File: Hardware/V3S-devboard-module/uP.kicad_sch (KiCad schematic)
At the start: 11 parts, among them U1 V3S, Y1 Crystal_GND23_Small, Y2 Crystal_GND23_Small

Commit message: schematic improvements
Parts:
- added C45, C46: 1u, symbol Device:C_Small
- added J2: Micro_SD_Card_Det1, v3s-devboard-module:J_sd_micro_socket, symbol Connector:Micro_SD_Card_Det1
- added L4: 2.2u, symbol Device:L_Small
- added R15, R17: 10K, symbol Device:R_Small_US
- added R16: 47K, symbol Device:R_Small_US
- added RN1: 6x47K, Resistor_THT:R_Array_SIP7, symbol Device:R_Pack06
- added SW1: SW_MEC_5E, mod:SW_SKRPACE010, symbol Switch:SW_MEC_5E
- added U4: W25Q128JVS, Package_SO:SOIC-8_5.23x5.23mm_P1.27mm, symbol Memory_Flash:W25Q128JVS
- added U5: AP3019AKTR-G1, Package_TO_SOT_SMD:SOT-23-6, symbol v3s-devboard-module:AP3019AKTR-G1
- U1: footprint Package_QFP:LQFP-128_14x14mm_P0.4mm -> v3s-devboard-module:LQFP-128_L14.0-W14.0-P0.40-LS16.0-BL-EP5.0
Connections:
- net GND: now also C45.1, C46.1, J2.6 (VSS), R17.1, SW1.3 (K), U4.4 (GND), U5.2 (GND)
- net PF0_SDC0D1_JTAGDI1: now also J2.8 (DAT1), RN1.5 (R5.1)
- net PF1_SDC0D0_JTAGDI1: now also J2.7 (DAT0), RN1.4 (R4.1)
- net PF2_SDC0CLK_UART0TX: now also J2.5 (CLK)
- net PF3_SDC0CMD_JTAGDO1: now also J2.3 (CMD), RN1.3 (R3.1)
- net PF4_SDC0D3_UART0RX: now also J2.2 (DAT3/CD), RN1.2 (R2.1)
- net PF5_SDC0D2_JTAGCK1: now also J2.1 (DAT2), RN1.1 (R1.1)
- net PF6: now also J2.9 (DET), RN1.6 (R6.1)
- net SPI.CLK: now also U4.6 (CLK)
- net SPI.CS: now also R15.1, U4.1 (~{CS})
- net SPI.MISO: now also U4.2 (DO(IO1))
- net SPI.MOSI: now also U4.5 (DI(IO0))
- net UART2.RTS renamed PB2
- net PB2: now also R17.2, U5.4 (CTRL)
- new net: L4.2, U5.1 (SW)
- new net: C46.2, L4.1, U5.6 (VIN)
- new net: C45.2, R16.2, SW1.2
- new net 3V3: J2.4 (VDD), R15.2, R16.1, RN1.10 (R3.2), RN1.11 (R2.2), RN1.12 (R1.2), RN1.7 (R6.2), RN1.8 (R5.2), RN1.9 (R4.2), U4.3 (IO2), U4.7 (IO3), U4.8 (VCC)
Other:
- moved on the sheet: R8, U1

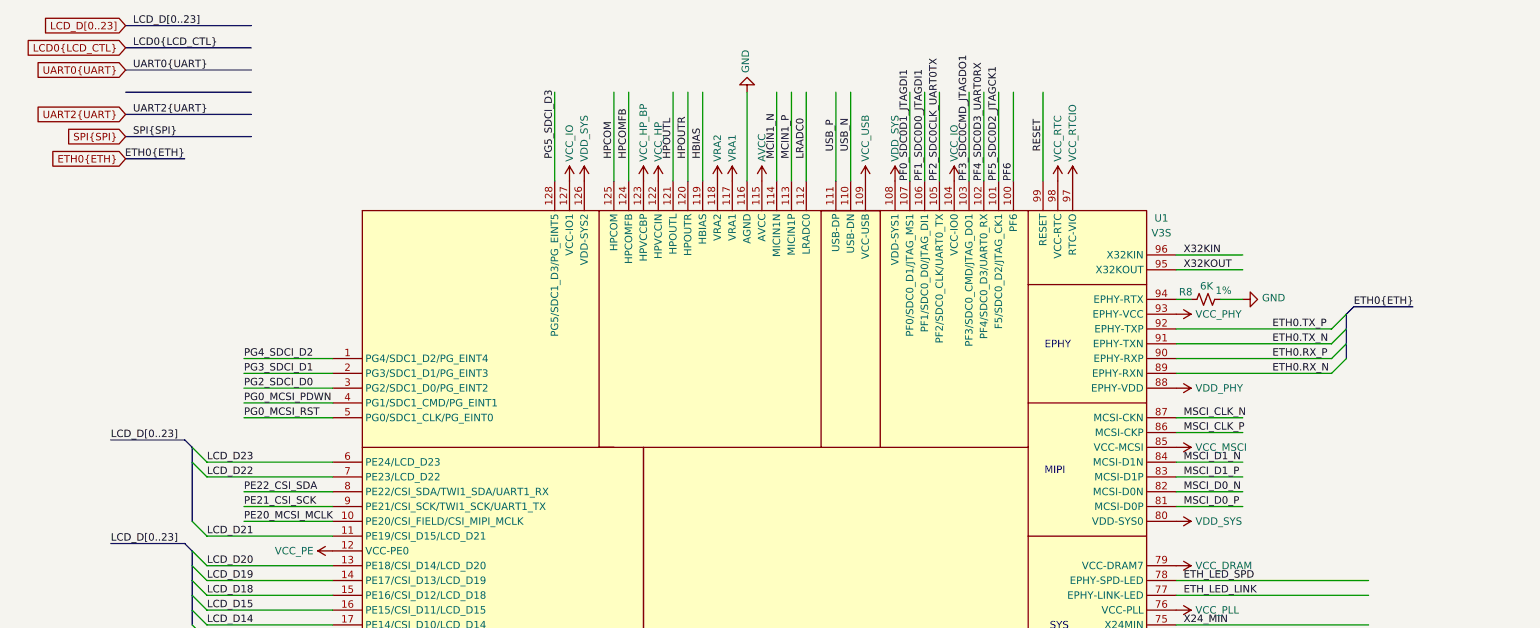
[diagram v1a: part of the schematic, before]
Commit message: Removed old project. Schematic improvements
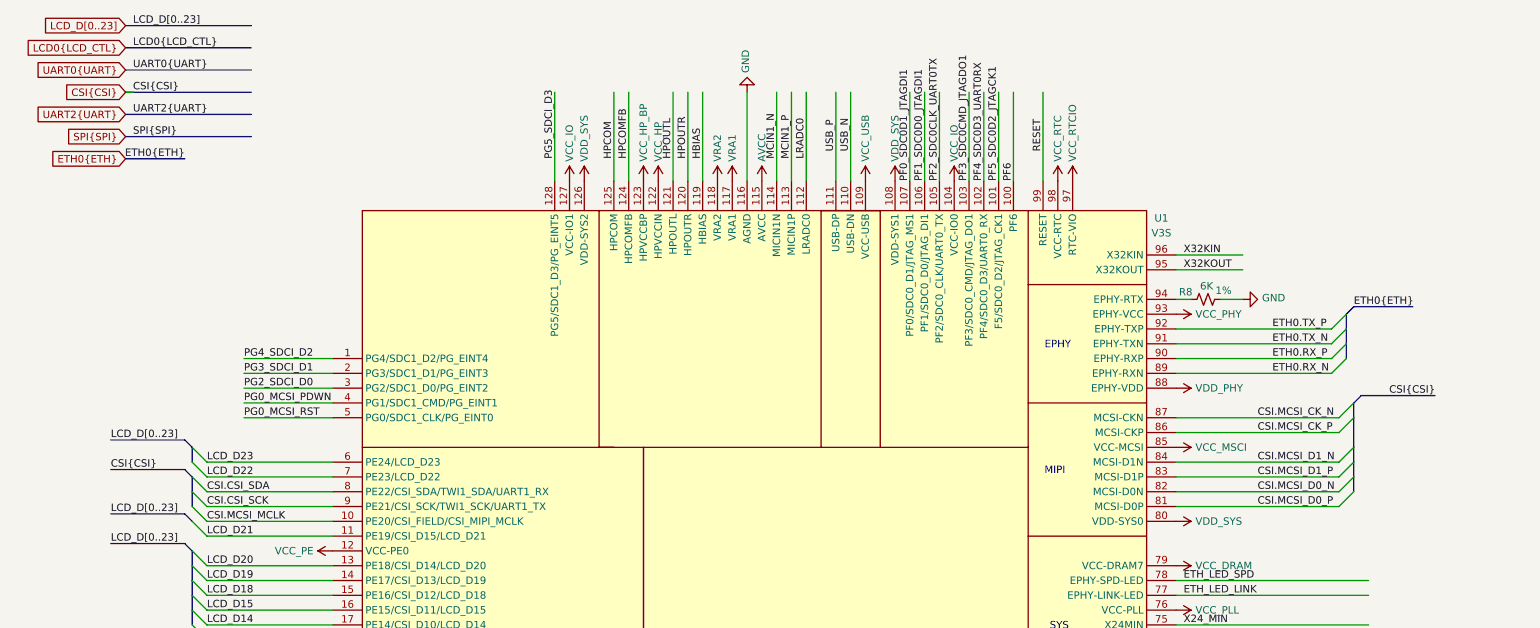
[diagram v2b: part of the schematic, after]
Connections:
- net MSCI_CLK_N renamed CSI.MCSI_CK_N
- net MSCI_CLK_P renamed CSI.MCSI_CK_P
- net MSCI_D0_N renamed CSI.MCSI_D0_N
- net MSCI_D0_P renamed CSI.MCSI_D0_P
- net MSCI_D1_N renamed CSI.MCSI_D1_N
- net MSCI_D1_P renamed CSI.MCSI_D1_P
- net PE20_MCSI_MCLK renamed CSI.MCSI_MCLK
- net PE21_CSI_SCK renamed CSI.CSI_SCK
- net PE22_CSI_SDA renamed CSI.CSI_SDA

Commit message: general improvements. power almost complete
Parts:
- removed C46: 1u, symbol Device:C_Small
- removed L4: 2.2u, symbol Device:L_Small
- removed R17: 10K, symbol Device:R_Small_US
- removed U5: AP3019AKTR-G1, Package_TO_SOT_SMD:SOT-23-6, symbol v3s-devboard-module:AP3019AKTR-G1
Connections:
- net PF0_SDC0D1_JTAGDI1: no longer U1.107 (PF0/SDC0_D1/JTAG_MS1)
- net PF1_SDC0D0_JTAGDI1: no longer U1.106 (PF1/SDC0_D0/JTAG_DI1)
- net PF2_SDC0CLK_UART0TX: no longer U1.105 (PF2/SDC0_CLK/UART0_TX)
- net PF3_SDC0CMD_JTAGDO1: no longer U1.103 (PF3/SDC0_CMD/JTAG_DO1)
- net PF4_SDC0D3_UART0RX: no longer U1.102 (PF4/SDC0_D3/UART0_RX)
- net PF5_SDC0D2_JTAGCK1: no longer U1.101 (F5/SDC0_D2/JTAG_CK1)
- net RESET: now also C45.2, R16.2, SW1.2
- net PG0_MCSI_PDWN renamed SDC1.CMD
- net PG0_MCSI_RST renamed SDC1.CLK
- net PG2_SDCI_D0 renamed SDC1.D0
- net PG3_SDCI_D1 renamed SDC1.D1
- net PG4_SDCI_D2 renamed SDC1.D2
- net USB_N renamed USB.USB_N
- net USB_P renamed USB.USB_P
- new net SDC0.CLK: U1.105 (PF2/SDC0_CLK/UART0_TX)
- new net SDC0.CMD: U1.103 (PF3/SDC0_CMD/JTAG_DO1)
- new net SDC0.D0: U1.106 (PF1/SDC0_D0/JTAG_DI1)
- new net SDC0.D1: U1.107 (PF0/SDC0_D1/JTAG_MS1)
- new net SDC0.D2: U1.101 (F5/SDC0_D2/JTAG_CK1)
- new net SDC0.D3: U1.102 (PF4/SDC0_D3/UART0_RX)
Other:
- note added: "Interfaces: 1xParallel LCD (24bit+ctl) 2xUART 1xSPI 1xCSI (Camera Serial Interface) 2xSDC 1xETH 1xUSB"
- note added: "Use AP3019AKTR-G1 for LCD backlight generation"
- moved on the sheet: R8, U1

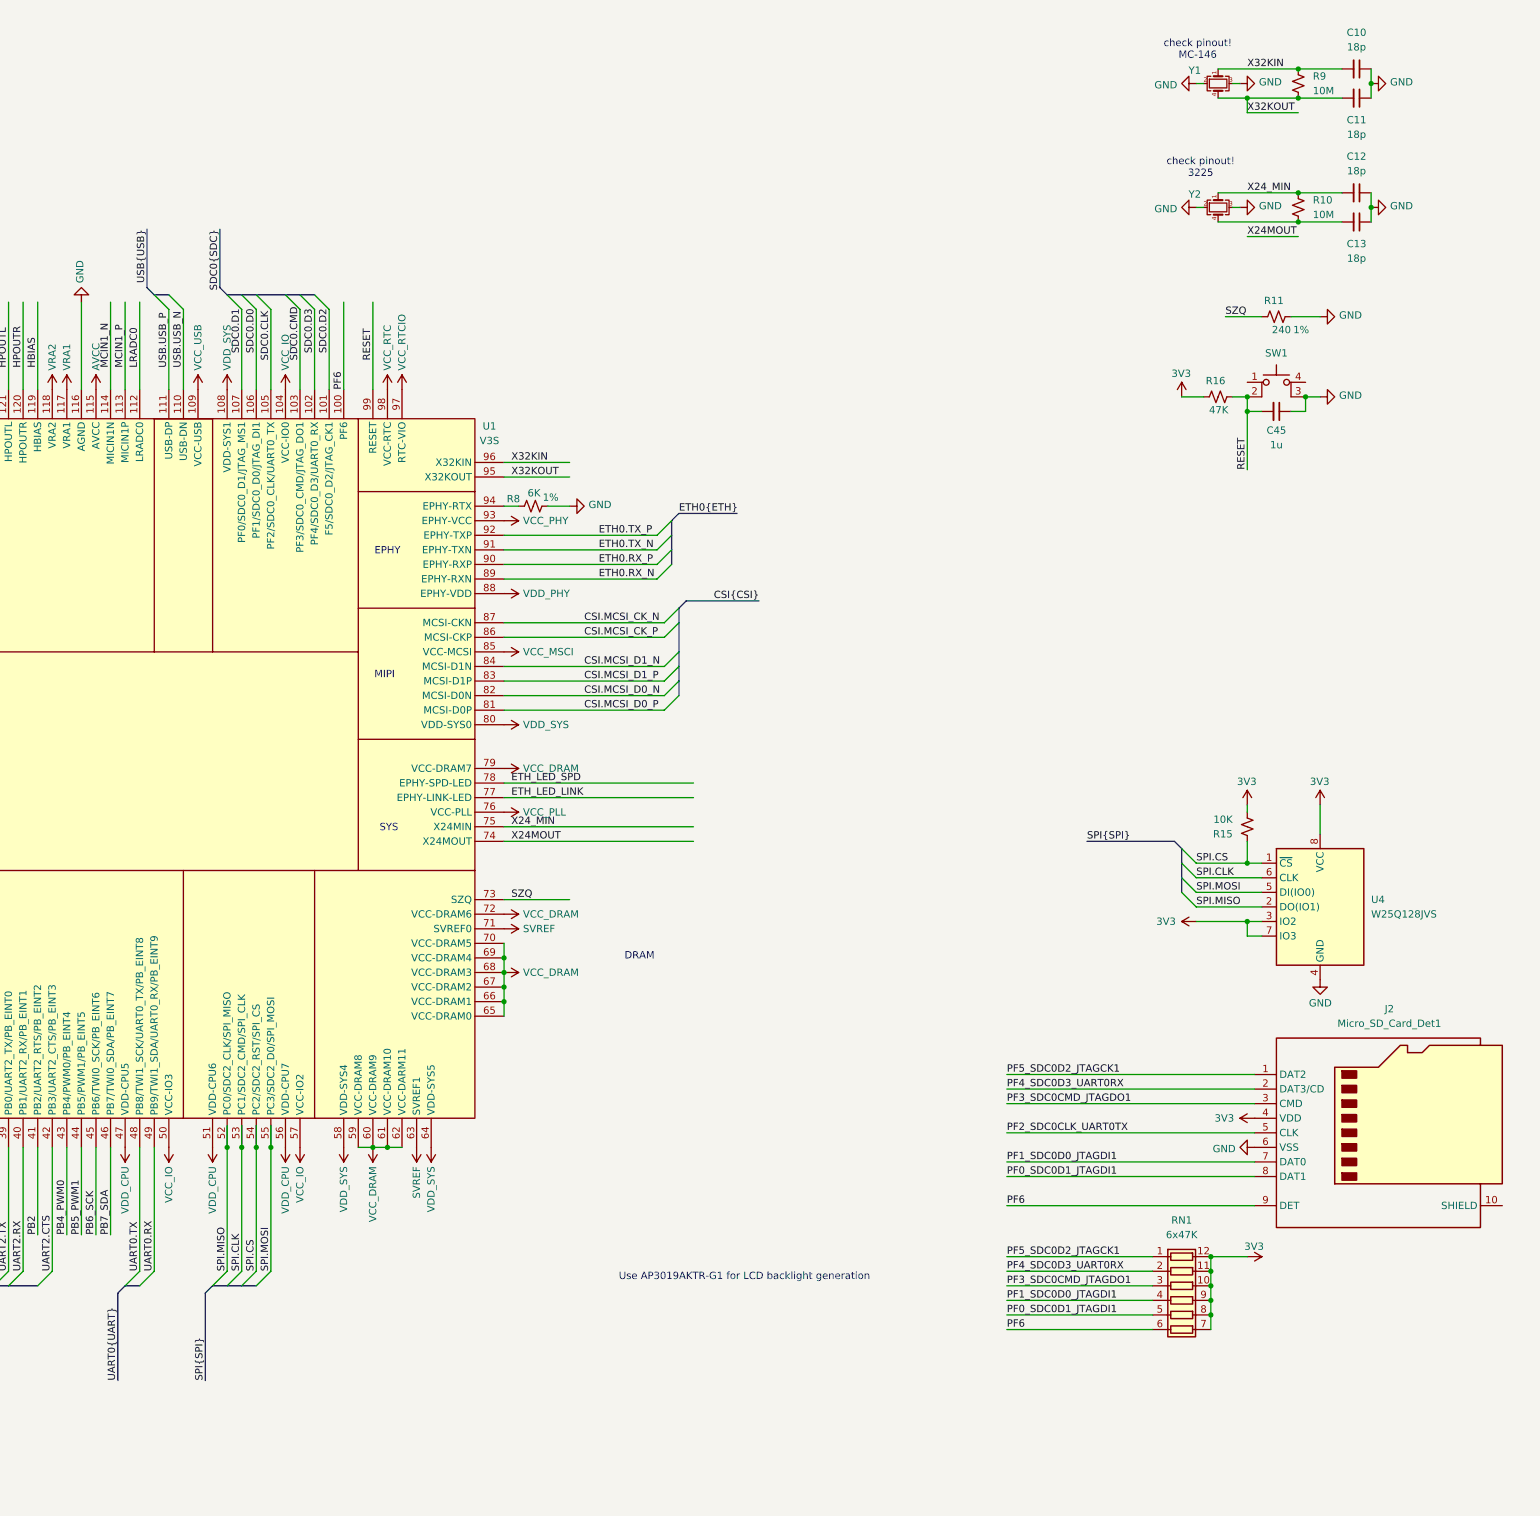
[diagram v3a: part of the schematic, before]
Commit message: CPU schematic improvements
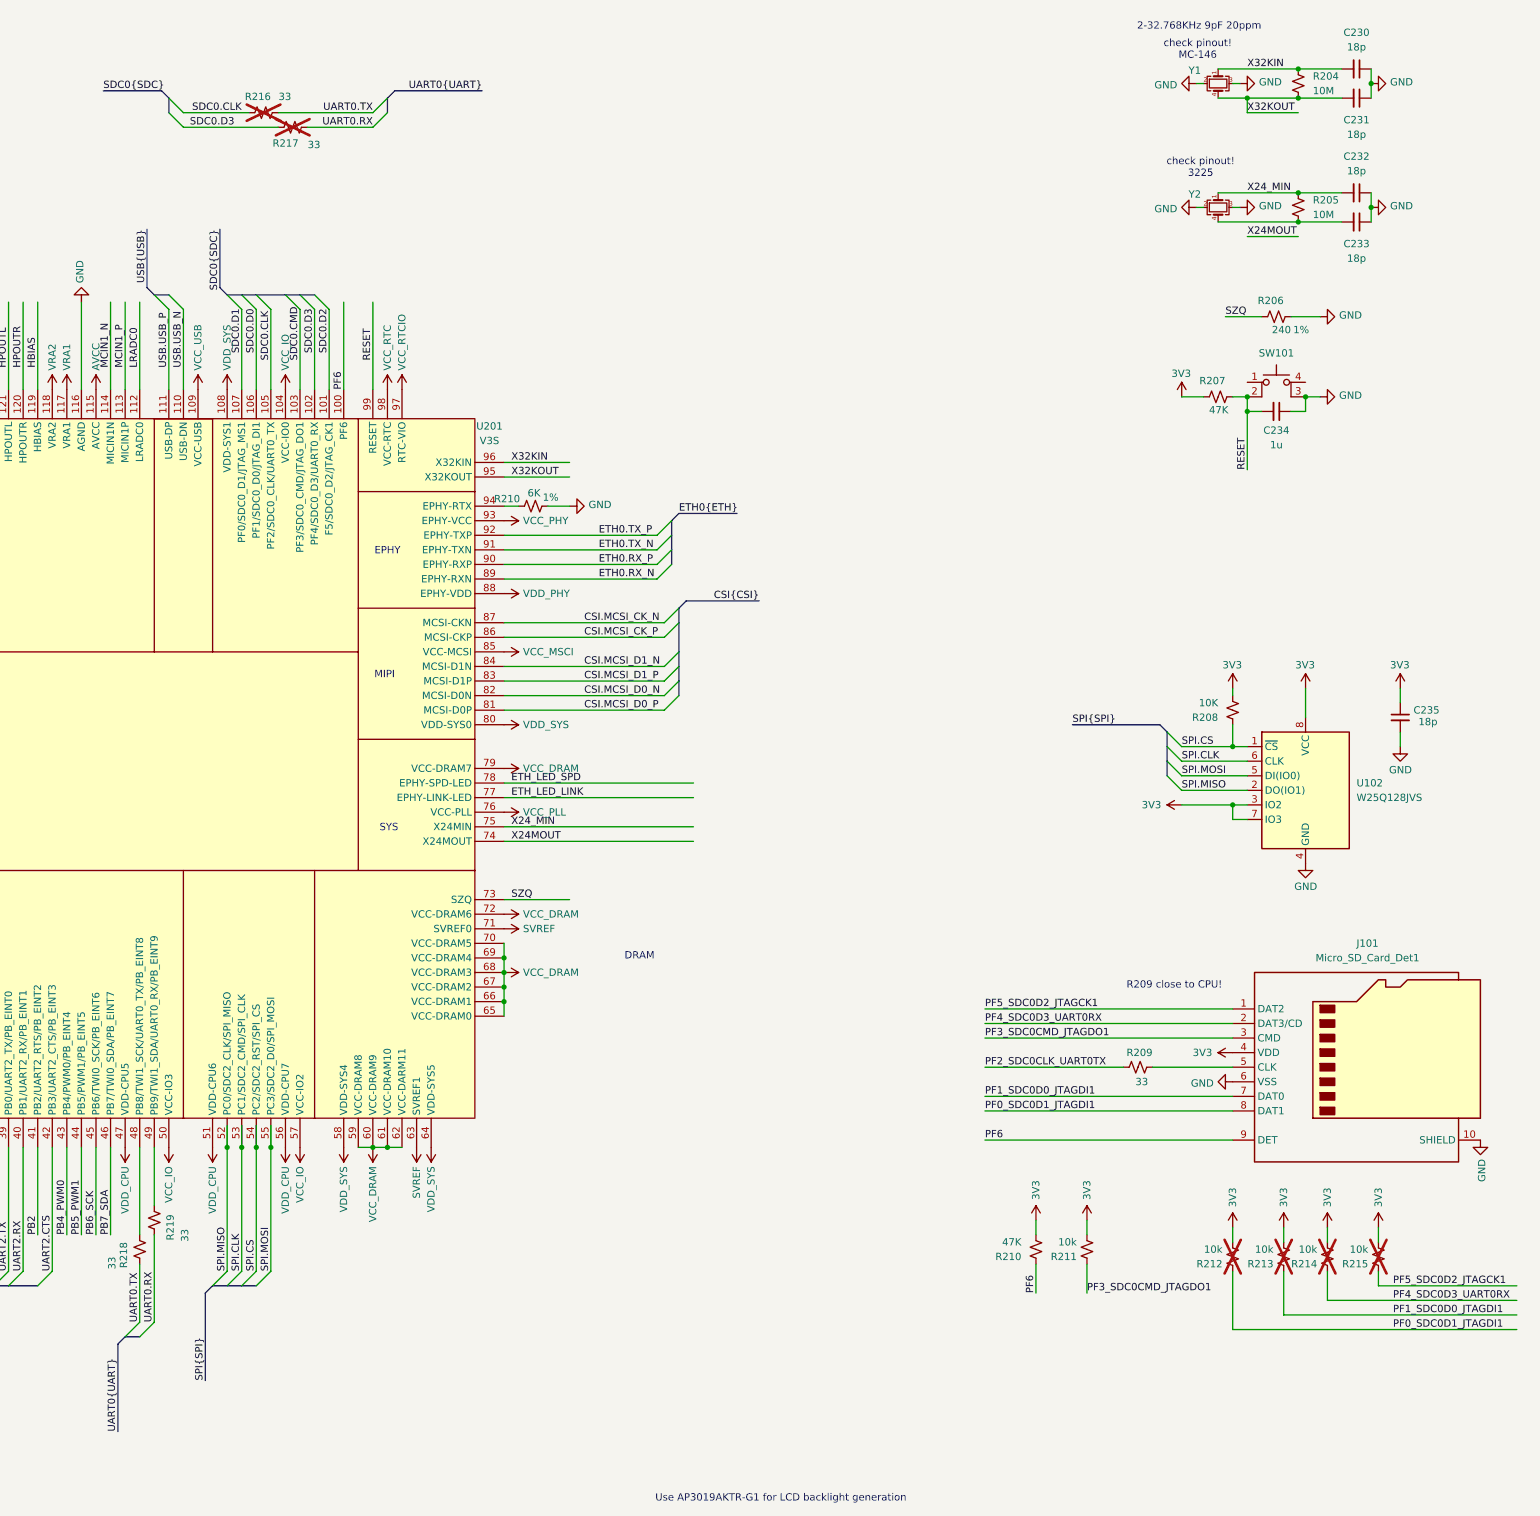
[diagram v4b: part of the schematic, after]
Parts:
- removed RN1: 6x47K, Resistor_THT:R_Array_SIP7, symbol Device:R_Pack06
- added C235: 18p, Capacitor_SMD:C_0603_1608Metric, symbol Device:C_Small
- added R209, R216, R217, R218, R219: 33, Resistor_SMD:R_0603_1608Metric, symbol Device:R_Small_US
- added R210: 47K, Resistor_SMD:R_0603_1608Metric, symbol Device:R_Small_US
- added R211, R212, R213, R214, R215: 10k, Resistor_SMD:R_0603_1608Metric, symbol Device:R_Small_US
- C230: renamed from C10; footprint (none) -> Capacitor_SMD:C_0603_1608Metric
- C231: renamed from C11; footprint (none) -> Capacitor_SMD:C_0603_1608Metric
- C232: renamed from C12; footprint (none) -> Capacitor_SMD:C_0603_1608Metric
- C233: renamed from C13; footprint (none) -> Capacitor_SMD:C_0603_1608Metric
- C234: renamed from C45; footprint (none) -> Capacitor_SMD:C_0603_1608Metric
- R204: renamed from R9; footprint (none) -> Resistor_SMD:R_0603_1608Metric
- R205: renamed from R10; footprint (none) -> Resistor_SMD:R_0603_1608Metric
- R206: renamed from R11; footprint (none) -> Resistor_SMD:R_0603_1608Metric
- R207: renamed from R16; footprint (none) -> Resistor_SMD:R_0603_1608Metric
- R208: renamed from R15; footprint (none) -> Resistor_SMD:R_0603_1608Metric
- renumbered J2 to J101, R8 to R210, SW1 to SW101, U4 to U102, U1 to U201
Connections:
- net 3V3: now also C235.1, R210.2, R211.2, R212.2, R213.2, R214.2, R215.2
- net GND: now also J101.10 (SHIELD), C235.2
- net PF0_SDC0D1_JTAGDI1: now also R212.1
- net PF1_SDC0D0_JTAGDI1: now also R213.1
- net PF2_SDC0CLK_UART0TX: now also R209.1; no longer J101.5 (CLK)
- net PF3_SDC0CMD_JTAGDO1: now also R211.1
- net PF4_SDC0D3_UART0RX: now also R214.1
- net PF5_SDC0D2_JTAGCK1: now also R215.1
- net PF6: now also R210.1
- net SDC0.CLK: now also R216.1
- net SDC0.D3: now also R217.1
- net UART0.RX: now also R217.2, R219.1; no longer U201.49 (PB9/TWI1_SDA/UART0_RX/PB_EINT9)
- net UART0.TX: now also R216.2, R218.1; no longer U201.48 (PB8/TWI1_SCK/UART0_TX/PB_EINT8)
- new net: R218.2, U201.48 (PB8/TWI1_SCK/UART0_TX/PB_EINT8)
- new net: R219.2, U201.49 (PB9/TWI1_SDA/UART0_RX/PB_EINT9)
- new net: J101.5 (CLK), R209.2
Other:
- note added: "2-32.768KHz 9pF 20ppm"
- note added: "R209 close to CPU!"
- moved on the sheet: J101, R208, U102
